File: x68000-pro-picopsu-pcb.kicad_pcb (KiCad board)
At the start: 2 copper layers, 209 x 98 mm, 21 parts, among them J1 Fan Header, J2 Screw_Terminal_01x07, J3 Screw_Terminal_01x07, J4 PicoPSU, U1 74LS04

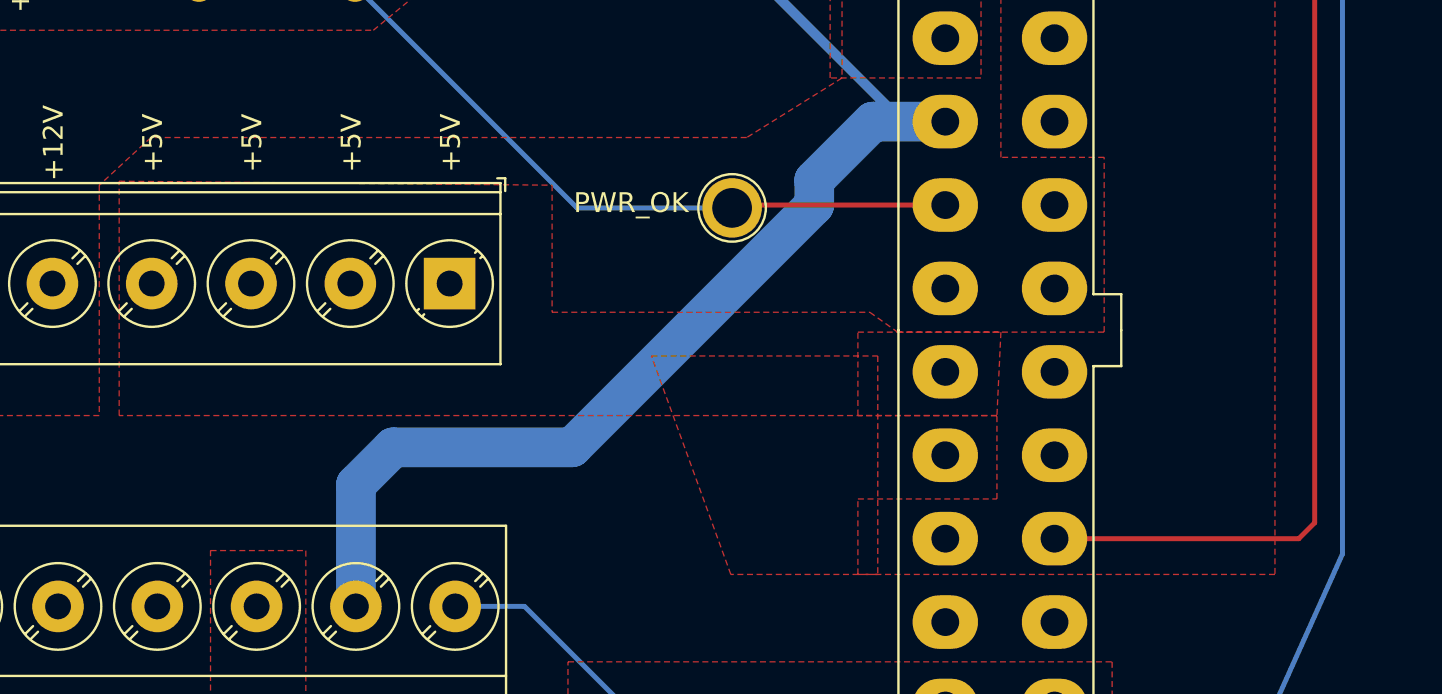
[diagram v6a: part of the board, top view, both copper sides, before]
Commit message: Clean up some pad confusion
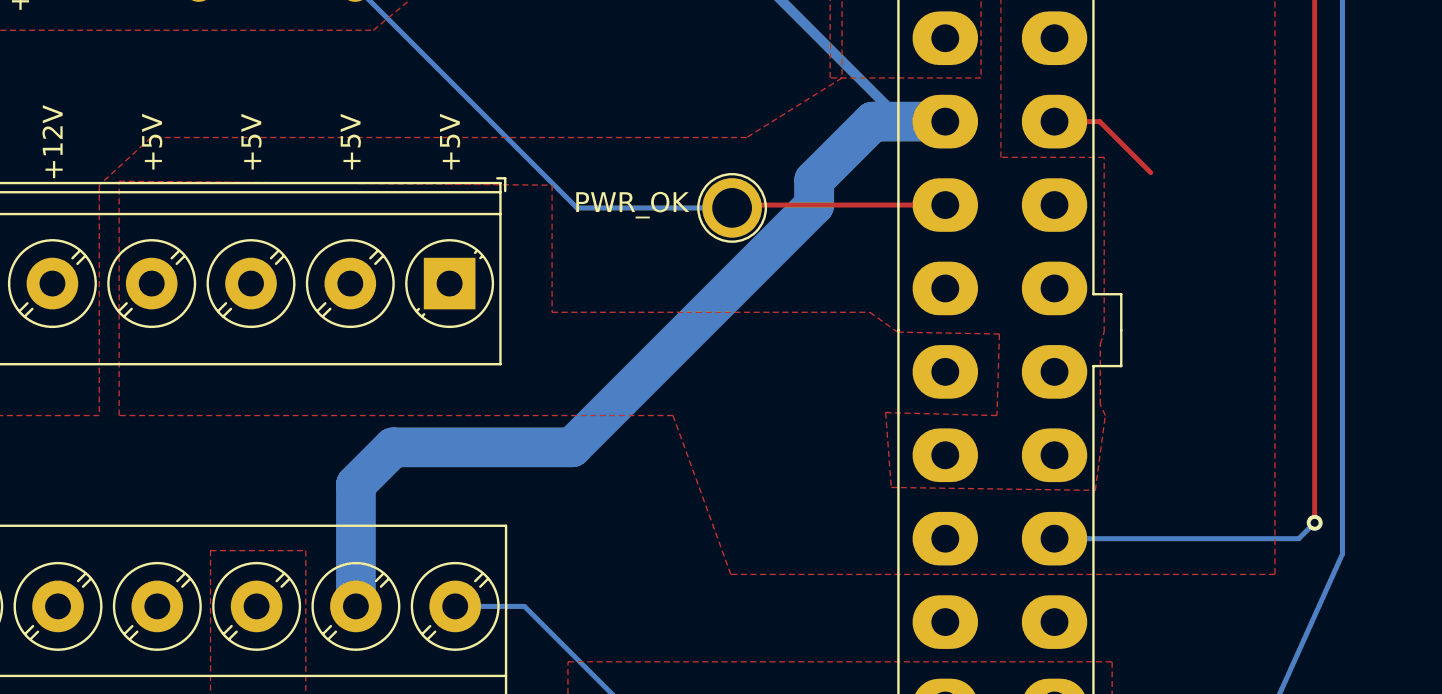
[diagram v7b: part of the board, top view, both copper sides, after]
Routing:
- net /PSU_5V: track 0.00 -> 5.91 mm
- net /~PS_ON: vias 0 -> 1
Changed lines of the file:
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@@
     (thickness 1.6)
     (drawings 43)
-    (tracks 51)
+    (tracks 55)
     (zones 0)
     (modules 21)
@@
   )
   (setup
-    (last_trace_width 2)
+    (last_trace_width 0.25)
     (user_trace_width 0.5)
     (user_trace_width 2)
@@
   (segment (start 106.097 84.297) (end 109.6 87.8) (width 0.25) (layer F.Cu) (net 6))
   (segment (start 109.6 87.8) (end 109.6 126.6) (width 0.25) (layer F.Cu) (net 6))
-  (segment (start 108.8 127.4) (end 96.5 127.4) (width 0.25) (layer F.Cu) (net 6) (status 20))
-  (segment (start 109.6 126.6) (end 108.8 127.4) (width 0.25) (layer F.Cu) (net 6))
+  (segment (start 109.6 126.6) (end 109.6 126.6) (width 0.25) (layer F.Cu) (net 6))
+  (via (at 109.6 126.6) (size 0.8) (drill 0.4) (layers F.Cu B.Cu) (net 6))
+  (segment (start 108.8 127.4) (end 109.6 126.6) (width 0.25) (layer B.Cu) (net 6))
+  (segment (start 96.5 127.4) (end 108.8 127.4) (width 0.25) (layer B.Cu) (net 6))
   (segment (start 96.5 135.5) (end 96.5 135.8) (width 0.5) (layer F.Cu) (net 7) (status 30))
   (segment (start 80.264 97.814) (end 80.264 92) (width 0.5) (layer B.Cu) (net 10) (status 20))
@@
   (segment (start 80.408 110.6) (end 80.264 110.744) (width 0.25) (layer F.Cu) (net 11))
   (segment (start 91 110.6) (end 80.408 110.6) (width 0.25) (layer F.Cu) (net 11))
+  (segment (start 96.5 106.4) (end 98.78 106.4) (width 0.25) (layer F.Cu) (net 12))
+  (segment (start 98.78 106.4) (end 101.346 108.966) (width 0.25) (layer F.Cu) (net 12))
   (segment (start 69.81 130.81) (end 82 143) (width 0.25) (layer B.Cu) (net 15) (status 20))
   (segment (start 66.322 130.81) (end 69.81 130.81) (width 0.25) (layer B.Cu) (net 15) (status 10))
@@
     (polygon
       (pts
-        (xy 107.6 129.2) (xy 86.6 129.2) (xy 86.6 125.4) (xy 93.6 125.4) (xy 93.6 121.2)
-        (xy 86.6 121.2) (xy 86.6 117) (xy 99 117) (xy 99 108.2) (xy 93.8 108.2)
+        (xy 107.6 129.2) (xy 80.2 129.2) (xy 77.290909 121.2) (xy 49.4 121.2) (xy 49.4 109.4)
+        (xy 71.2 109.6) (xy 71.2 116) (xy 87.2 116) (xy 88.6 117) (xy 93.726 117.094)
+        (xy 93.6 121.2) (xy 87.996 121.052) (xy 88.28 124.82) (xy 98.552 124.968) (xy 99.06 121.2)
+        (xy 98.806 120.65) (xy 98.806 117.602) (xy 99 117) (xy 99 108.2) (xy 93.8 108.2)
         (xy 93.8 96) (xy 107.6 96)
       )
     )
-  )
-  (zone (net 12) (net_name /PSU_5V) (layer F.Cu) (hatch edge 0.508)
-    (connect_pads (clearance 0.508))
-    (min_thickness 0.254)
-    (fill yes (arc_segments 32) (thermal_gap 0.508) (thermal_bridge_width 0.508))
-    (polygon
-      (pts
-        (xy 71.2 116) (xy 87.2 116) (xy 88.6 117) (xy 93.8 117) (xy 93.6 121.2)
-        (xy 49.4 121.2) (xy 49.4 109.4) (xy 71.2 109.6)
-      )
-    )
-  )
-  (zone (net 12) (net_name /PSU_5V) (layer F.Cu) (hatch edge 0.508)
-    (connect_pads (clearance 0.508))
-    (min_thickness 0.254)
-    (fill yes (arc_segments 32) (thermal_gap 0.508) (thermal_bridge_width 0.508))
-    (polygon
-      (pts
-        (xy 87.6 129.2) (xy 80.2 129.2) (xy 76.2 118.2) (xy 87.6 118.2)
-      )
-    )

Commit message: Rust logo
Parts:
- added G***: LOGO, logos:fe2o3, B.Cu at (200.4, 144.8)
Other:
- board text added: "brought to you by"
- board text added: "special thanks: mattsoft for the x68000 og picopsu board"
